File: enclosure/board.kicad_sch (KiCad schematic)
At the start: 10 parts, among them J1 61900411021, J3 2x7, J4 02x17, J5 629105150521, SW1 SW_DPDT_x2

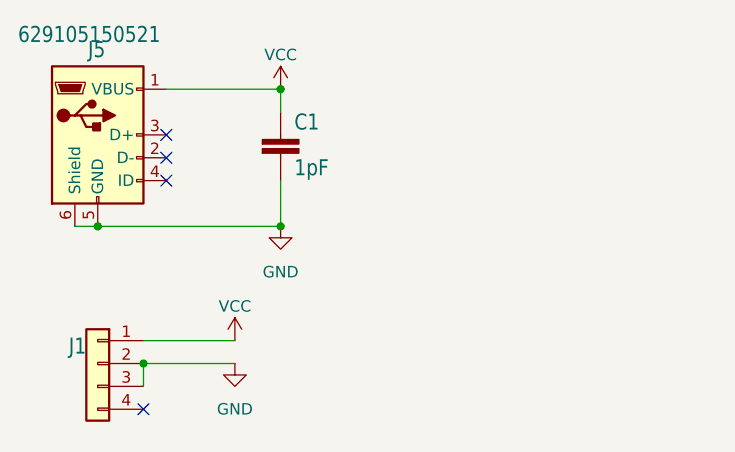
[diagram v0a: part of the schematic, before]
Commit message: Fix cap value, thicker text, and minor layout tweaks
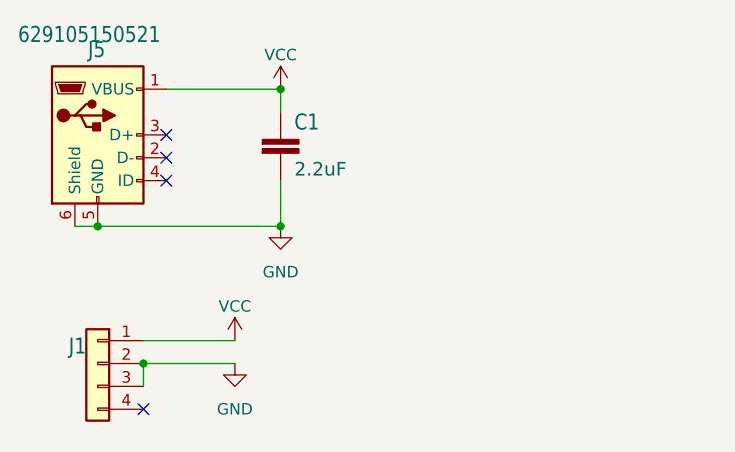
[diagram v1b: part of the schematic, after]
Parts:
- C1: value 1pF -> 2.2uF
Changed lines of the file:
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@@
-(kicad_sch (version 20210126) (generator eeschema)
+(kicad_sch (version 20210406) (generator eeschema)
   (paper "A4")
   (junction (at 53.34 86.36) (diameter 0.9144) (color 0 0 0 0))
@@
       (effects (font (size 1.778 1.5113)) (justify left bottom))
     )
-    (property "Value" "1pF" (id 1) (at 75.184 80.899 0)
-      (effects (font (size 1.778 1.5113)) (justify left bottom))
+    (property "Value" "2.2uF" (id 1) (at 75.184 80.899 0)
+      (effects (font (size 1.5113 1.5113)) (justify left bottom))
     )
     (property "Footprint" "Capacitor_SMD:C_0603_1608Metric" (id 2) (at 73.66 76.2 0)
@@
     )
     (path "/b2bfe2ef-2f69-49f8-9c51-d69fc4022c7e"
-      (reference "C1") (unit 1) (value "1pF") (footprint "Capacitor_SMD:C_0603_1608Metric")
+      (reference "C1") (unit 1) (value "2.2uF") (footprint "Capacitor_SMD:C_0603_1608Metric")
     )
     (path "/34f6a6cd-075f-4b6c-9fff-88464df18afc"

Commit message: initial v2 tweaks
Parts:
- added D? (x3): LED, symbol Device:LED
- added J?: Jack-DC, symbol Connector:Jack-DC
- added R?: 1.7k, symbol Device:R
- added R?: 3.3k, symbol Device:R
- added R?: 10k, symbol Device:R
- added R?: 3.8k, symbol Device:R
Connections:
- net GND: now also J?.2, R?.2, R?.2
- net +12V: now reaches J1.4 (Pin_4)
- net +12V: now also J?.1, R?.1
- net VCC renamed +5V
- net +5V: now also R?.1, R?.1, R?.2
- new net +3V3: R?.1, R?.2
- no-connect marks 10 -> 9
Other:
- moved on the sheet: H2, H4
